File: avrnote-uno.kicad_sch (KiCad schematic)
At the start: 42 parts, among them J1 VCCSEL, J2 DC, J3 USB_C_Recept_USB2.0, J4 Power, J5 Digital/PWM, J6 Analog, J7 Digital/PWM, SW1 SW_Reset, U1 AZ1117CH2-3.3, U2 NJM7805SDL1, U3 CH340E, U4 74AHC1G125, U5 ATmega328P-P, Y1 16MHz

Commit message: minorfix
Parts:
- Y1: footprint Crystal:Crystal_HC18-U_Vertical -> ATS08A-E:XTAL_HC49P488W43L1085T450H368
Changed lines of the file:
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@@
 			)
 		)
-		(property "Footprint" "Crystal:Crystal_HC18-U_Vertical"
+		(property "Footprint" "ATS08A-E:XTAL_HC49P488W43L1085T450H368"
 			(at 260.35 25.4 0)
 			(hide yes)

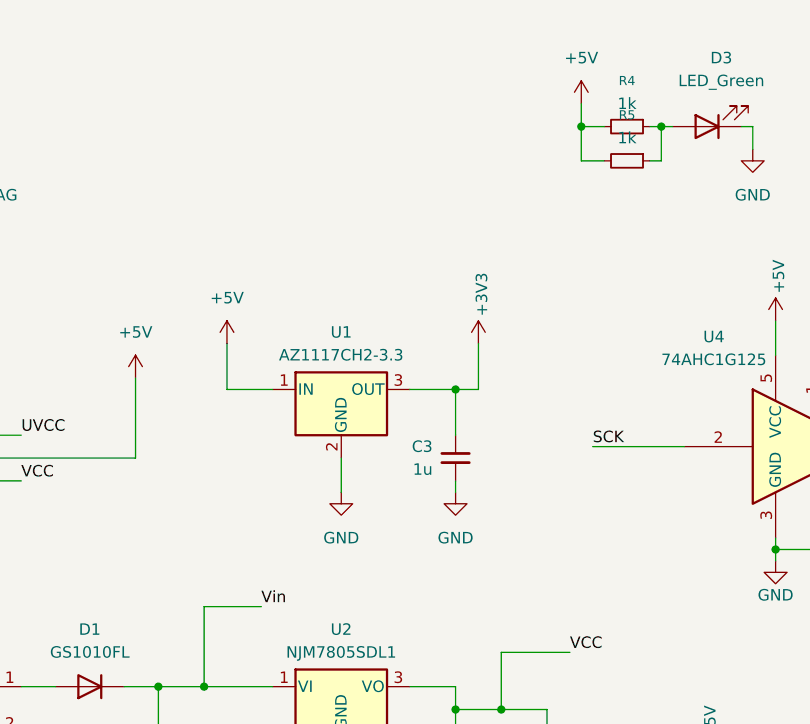
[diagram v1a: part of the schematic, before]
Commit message: fix: az1117ch2-3.3v -> az1117ch-3.3v
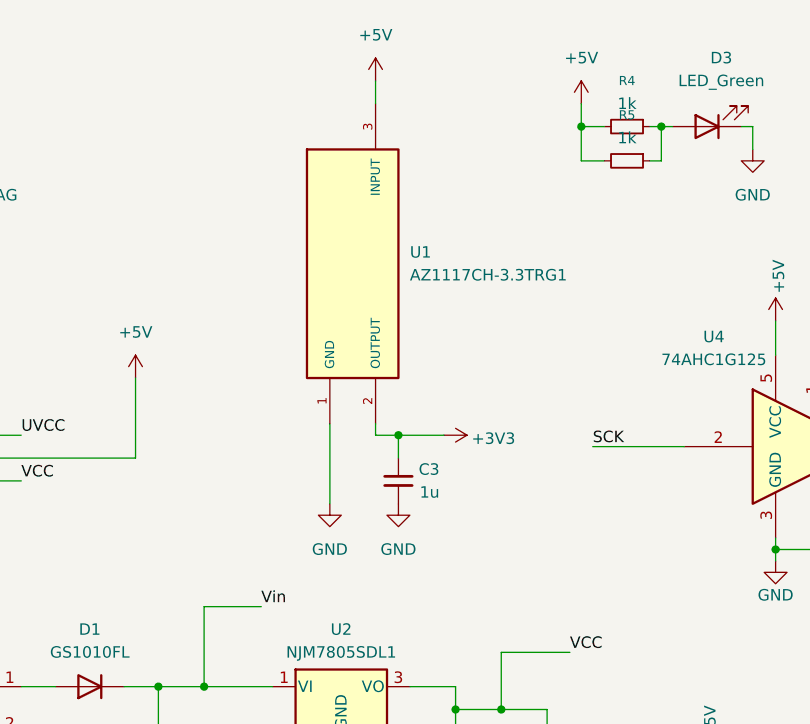
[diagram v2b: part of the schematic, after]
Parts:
- removed U1: AZ1117CH2-3.3, Package_TO_SOT_SMD:SOT-223-3_TabPin2, symbol Regulator_Linear:AZ1117CH2-3.3
- added U1: AZ1117CH-3.3TRG1, AZ1117CH-3.3TRG1:VREG_AZ1117CH-3.3TRG1, symbol AZ1117CH-3.3TRG1:AZ1117CH-3.3TRG1
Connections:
- net +3V3: now also U1.2 (OUTPUT), U1.4 (OUTPUT)
- net +5V: now also U1.3 (INPUT)
- net GND: now also U1.1 (GND)
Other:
- moved on the sheet: C3

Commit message: refactor
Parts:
- F1: footprint Inductor_SMD:L_TechFuse_SL0420 -> Fuse:Fuse_1206_3216Metric
- R10: footprint Resistor_THT:R_Axial_DIN0204_L3.6mm_D1.6mm_P5.08mm_Horizontal -> Resistor_SMD:R_0603_1608Metric
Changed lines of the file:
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@@
 			)
 		)
-		(property "Footprint" "Resistor_THT:R_Axial_DIN0204_L3.6mm_D1.6mm_P5.08mm_Horizontal"
+		(property "Footprint" "Resistor_SMD:R_0603_1608Metric"
 			(at 252.73 25.4 0)
 			(hide yes)
@@
 			)
 		)
-		(property "Footprint" "Inductor_SMD:L_TechFuse_SL0420"
+		(property "Footprint" "Fuse:Fuse_1206_3216Metric"
 			(at 54.61 124.46 0)
 			(hide yes)
